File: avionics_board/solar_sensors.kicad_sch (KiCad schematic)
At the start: 4 parts, among them U16 TCA9548APWR, U17 TCA9548APWR

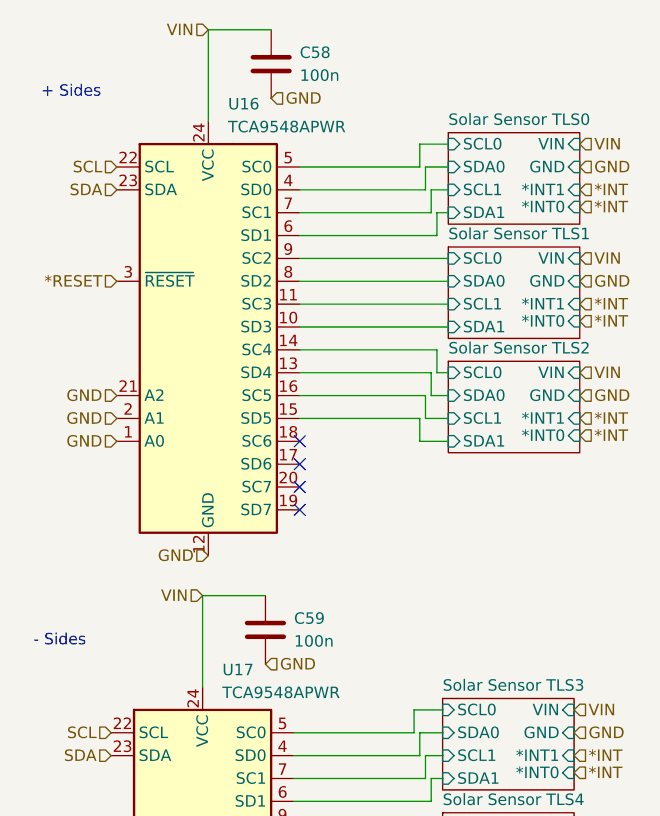
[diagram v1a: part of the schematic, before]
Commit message: reconcile BOMS for AVI. SCI and AUX
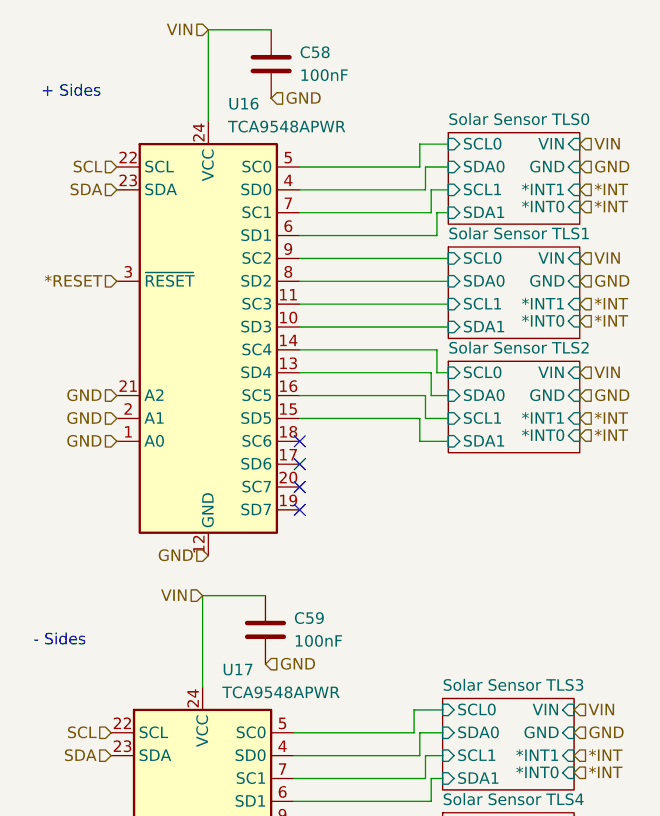
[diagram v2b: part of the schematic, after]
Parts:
- C58, C59: value 100n -> 100nF; Manufacturer (none) -> Murata; Part Number (none) -> GRM155R61E102KA01D; Tolerance (none) -> 10; Voltage (none) -> 25
- U16, U17: Manufacturer (none) -> TI; Part Number (none) -> TCA9548APWR
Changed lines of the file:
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@@
 			)
 		)
-		(property "Value" "100n"
+		(property "Value" "100nF"
 			(at 94.615 123.1899 0)
 			(effects
@@
 			)
 		)
-		(property "Datasheet" "~"
+		(property "Datasheet" "https://search.murata.co.jp/Ceramy/image/img/A01X/G101/ENG/GRM155R61E102KA01-01.pdf"
 			(at 91.44 121.92 0)
 			(effects
@@
 		)
 		(property "Alt" ""
+			(at 91.44 121.92 0)
+			(effects
+				(font
+					(size 1.27 1.27)
+				)
+				(hide yes)
+			)
+		)
+		(property "Manufacturer" "Murata"
+			(at 91.44 121.92 0)
+			(effects
+				(font
+					(size 1.27 1.27)
+				)
+				(hide yes)
+			)
+		)
+		(property "Part Number" "GRM155R61E102KA01D "
+			(at 91.44 121.92 0)
+			(effects
+				(font
+					(size 1.27 1.27)
+				)
+				(hide yes)
+			)
+		)
+		(property "Tolerance" "10"
+			(at 91.44 121.92 0)
+			(effects
+				(font
+					(size 1.27 1.27)
+				)
+				(hide yes)
+			)
+		)
+		(property "Voltage" "25"
 			(at 91.44 121.92 0)
 			(effects
@@
 			)
 		)
-		(property "Value" "100n"
+		(property "Value" "100nF"
 			(at 95.25 60.3249 0)
 			(effects
@@
 			)
 		)
-		(property "Datasheet" "~"
+		(property "Datasheet" "https://search.murata.co.jp/Ceramy/image/img/A01X/G101/ENG/GRM155R61E102KA01-01.pdf"
 			(at 92.075 59.055 0)
 			(effects
@@
 		)
 		(property "Alt" ""
+			(at 92.075 59.055 0)
+			(effects
+				(font
+					(size 1.27 1.27)
+				)
+				(hide yes)
+			)
+		)
+		(property "Manufacturer" "Murata"
+			(at 92.075 59.055 0)
+			(effects
+				(font
+					(size 1.27 1.27)
+				)
+				(hide yes)
+			)
+		)
+		(property "Part Number" "GRM155R61E102KA01D "
+			(at 92.075 59.055 0)
+			(effects
+				(font
+					(size 1.27 1.27)
+				)
+				(hide yes)
+			)
+		)
+		(property "Tolerance" "10"
+			(at 92.075 59.055 0)
+			(effects
+				(font
+					(size 1.27 1.27)
+				)
+				(hide yes)
+			)
+		)
+		(property "Voltage" "25"
 			(at 92.075 59.055 0)
 			(effects
@@
 			)
 		)
+		(property "Manufacturer" "TI"
+			(at 85.09 88.265 0)
+			(effects
+				(font
+					(size 1.27 1.27)
+				)
+				(hide yes)
+			)
+		)
+		(property "Part Number" "TCA9548APWR"
+			(at 85.09 88.265 0)
+			(effects
+				(font
+					(size 1.27 1.27)
+				)
+				(hide yes)
+			)
+		)
 		(pin "24"
 		)
@@
 			(at 84.455 151.13 0)
 			(effects
+				(font
+					(size 1.27 1.27)
+				)
+				(hide yes)
+			)
+		)
+		(property "Manufacturer" "TI"
+			(at 84.455 151.13 0)
+			(effects
+				(font
+					(size 1.27 1.27)
+				)
+				(hide yes)
+			)
+		)
+		(property "Part Number" "TCA9548APWR"
+			(at 84.455 151.13 0)
+			(effects

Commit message: interim checkin for EPS BOM
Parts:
- C58, C59: Part Number GRM155R61E102KA01D -> GRM155R61E104KA87D
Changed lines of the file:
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@@
 			)
 		)
-		(property "Datasheet" "https://search.murata.co.jp/Ceramy/image/img/A01X/G101/ENG/GRM155R61E102KA01-01.pdf"
+		(property "Datasheet" "https://search.murata.co.jp/Ceramy/image/img/A01X/G101/ENG/GRM155R61E104KA87-01.pdf"
 			(at 91.44 121.92 0)
 			(effects
@@
 			)
 		)
-		(property "Part Number" "GRM155R61E102KA01D "
+		(property "Part Number" "GRM155R61E104KA87D"
 			(at 91.44 121.92 0)
 			(effects
@@
 			)
 		)
-		(property "Datasheet" "https://search.murata.co.jp/Ceramy/image/img/A01X/G101/ENG/GRM155R61E102KA01-01.pdf"
+		(property "Datasheet" "https://search.murata.co.jp/Ceramy/image/img/A01X/G101/ENG/GRM155R61E104KA87-01.pdf"
 			(at 92.075 59.055 0)
 			(effects
@@
 			)
 		)
-		(property "Part Number" "GRM155R61E102KA01D "
+		(property "Part Number" "GRM155R61E104KA87D"
 			(at 92.075 59.055 0)
 			(effects

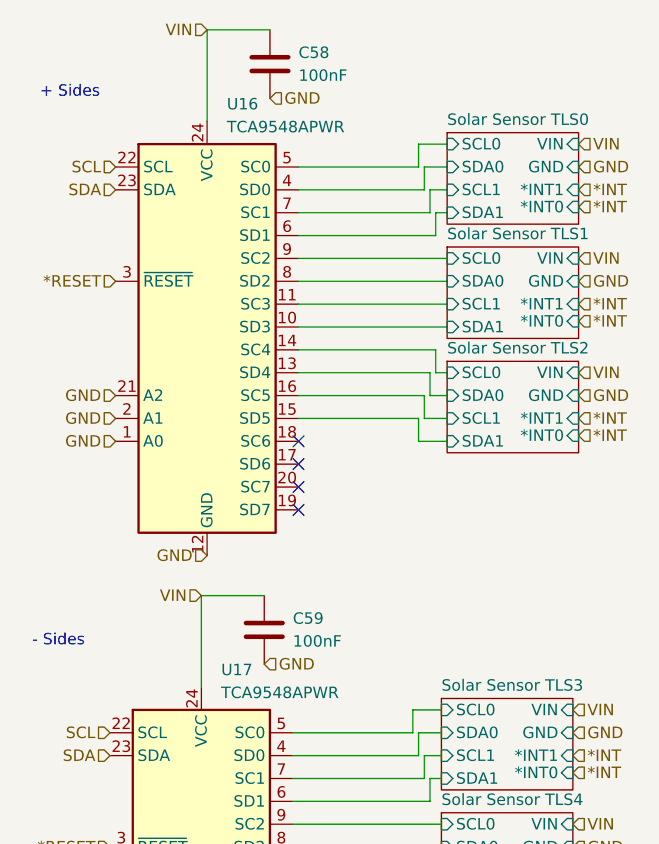
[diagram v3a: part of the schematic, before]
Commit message: reenumerate AVI board
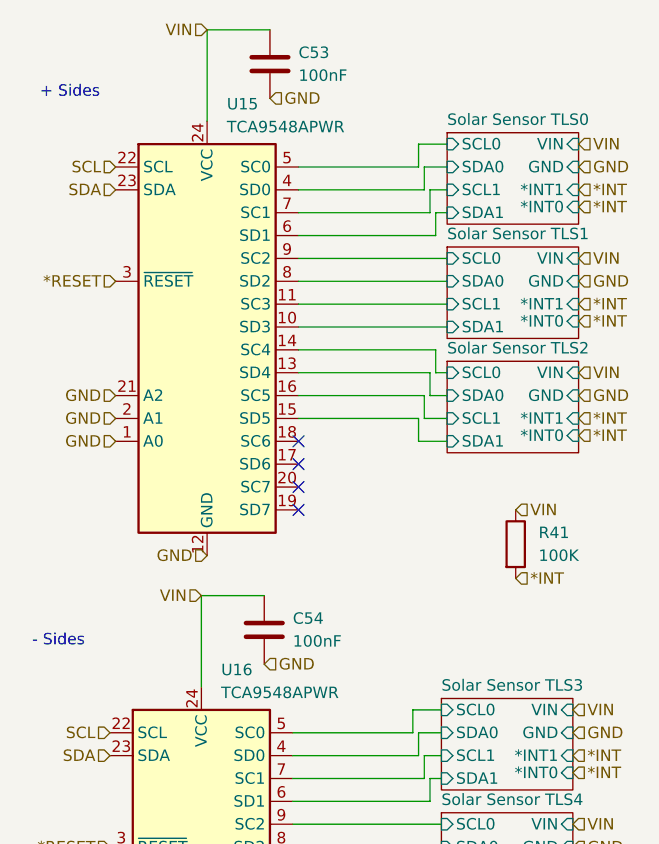
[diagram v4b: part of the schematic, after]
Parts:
- added R41: 100K, Resistor_SMD:R_0402_1005Metric_Pad0.72x0.64mm_HandSolder, symbol Device:R
- renumbered C58 to C53, C59 to C54, U16 to U15, U17 to U16
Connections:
- net *INT: now also R41.2
- net VIN: now also R41.1
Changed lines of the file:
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@@
+		)
+	)
+	(hierarchical_label "*INT"
+		(shape input)
+		(at 119.38 116.205 0)
+		(fields_autoplaced yes)
+		(effects
+			(font
+				(size 1.27 1.27)
+			)
+			(justify left)
 		)
 	)
@@
 		)
 	)
+	(hierarchical_label "VIN"
+		(shape input)
+		(at 119.38 108.585 0)
+		(fields_autoplaced yes)
+		(effects
+			(font
+				(size 1.27 1.27)
+			)
+			(justify left)
+		)
+	)
 	(hierarchical_label "*INT"
 		(shape input)
@@
 			)
 			(justify left)
+		)
+	)
+	(symbol
+		(lib_id "Device:R")
+		(at 119.38 112.395 0)
+		(unit 1)
+		(exclude_from_sim no)
+		(in_bom yes)
+		(on_board yes)
+		(dnp no)
+		(fields_autoplaced yes)
+		(property "Reference" "R41"
+			(at 121.92 111.1249 0)
+			(effects
+				(font
+					(size 1.27 1.27)
+				)
+				(justify left)
+			)
+		)
+		(property "Value" "100K"
+			(at 121.92 113.6649 0)
+			(effects
+				(font
+					(size 1.27 1.27)
+				)
+				(justify left)
+			)
+		)
+		(property "Footprint" "Resistor_SMD:R_0402_1005Metric_Pad0.72x0.64mm_HandSolder"
+			(at 117.602 112.395 90)
+			(effects
+				(font
+					(size 1.27 1.27)
+				)
+				(hide yes)
+			)
+		)
+		(property "Datasheet" "https://www.yageo.com/upload/media/product/products/datasheet/rchip/PYu-RC_Group_51_RoHS_L_12.pdf"
+			(at 119.38 112.395 0)
+			(effects
+				(font
+					(size 1.27 1.27)
+				)
+				(hide yes)
+			)
+		)
+		(property "Description" "Resistor"
+			(at 119.38 112.395 0)
+			(effects
+				(font
+					(size 1.27 1.27)
+				)
+				(hide yes)
+			)
+		)
+		(property "Manufacturer" "YAGEO"
+			(at 119.38 112.395 0)
+			(effects
+				(font
+					(size 1.27 1.27)
+				)
+				(hide yes)
+			)
+		)
+		(property "Part Number" "RC0402FR-07100KL"
+			(at 119.38 112.395 0)
+			(effects
+				(font
+					(size 1.27 1.27)
+				)
+				(hide yes)
+			)
+		)
+		(property "Tolerance" "1"
+			(at 119.38 112.395 0)
+			(effects
+				(font
+					(size 1.27 1.27)
+				)
+				(hide yes)
+			)
+		)
+		(pin "1"
+		)
+		(pin "2"
+		)
+		(instances
+			(project ""
+				(path "/f6cc00ab-17f1-4973-862f-7ac95fe70668/472a2b3c-f2e4-44b5-9587-658c9c0c9365"
+					(reference "R41")
+					(unit 1)
+				)
+			)
 		)
 	)
@@
 		(dnp no)
 		(fields_autoplaced yes)
-		(property "Reference" "C59"
+		(property "Reference" "C54"
 			(at 94.615 120.6499 0)
 			(effects
@@
 			(project "AVIONICS_BOARD"
 				(path "/f6cc00ab-17f1-4973-862f-7ac95fe70668/472a2b3c-f2e4-44b5-9587-658c9c0c9365"
-					(reference "C59")
+					(reference "C54")
 					(unit 1)
 				)
@@
 		(dnp no)
 		(fields_autoplaced yes)
-		(property "Reference" "C58"
+		(property "Reference" "C53"
 			(at 95.25 57.7849 0)
 			(effects
@@
 			(project "AVIONICS_BOARD"
 				(path "/f6cc00ab-17f1-4973-862f-7ac95fe70668/472a2b3c-f2e4-44b5-9587-658c9c0c9365"
-					(reference "C58")
+					(reference "C53")
 					(unit 1)
 				)
@@
 		(dnp no)
 		(fields_autoplaced yes)
-		(property "Reference" "U16"
+		(property "Reference" "U15"
 			(at 87.2841 63.5 0)
 			(effects
@@
 			(project "AVIONICS_BOARD"
 				(path "/f6cc00ab-17f1-4973-862f-7ac95fe70668/472a2b3c-f2e4-44b5-9587-658c9c0c9365"
-					(reference "U16")
+					(reference "U15")
 					(unit 1)
 				)
@@
 		(dnp no)
 		(fields_autoplaced yes)
-		(property "Reference" "U17"
+		(property "Reference" "U16"
 			(at 86.6491 126.365 0)
 			(effects
@@
 			(project "AVIONICS_BOARD"
 				(path "/f6cc00ab-17f1-4973-862f-7ac95fe70668/472a2b3c-f2e4-44b5-9587-658c9c0c9365"
-					(reference "U17")
+					(reference "U16")
 					(unit 1)
 				)

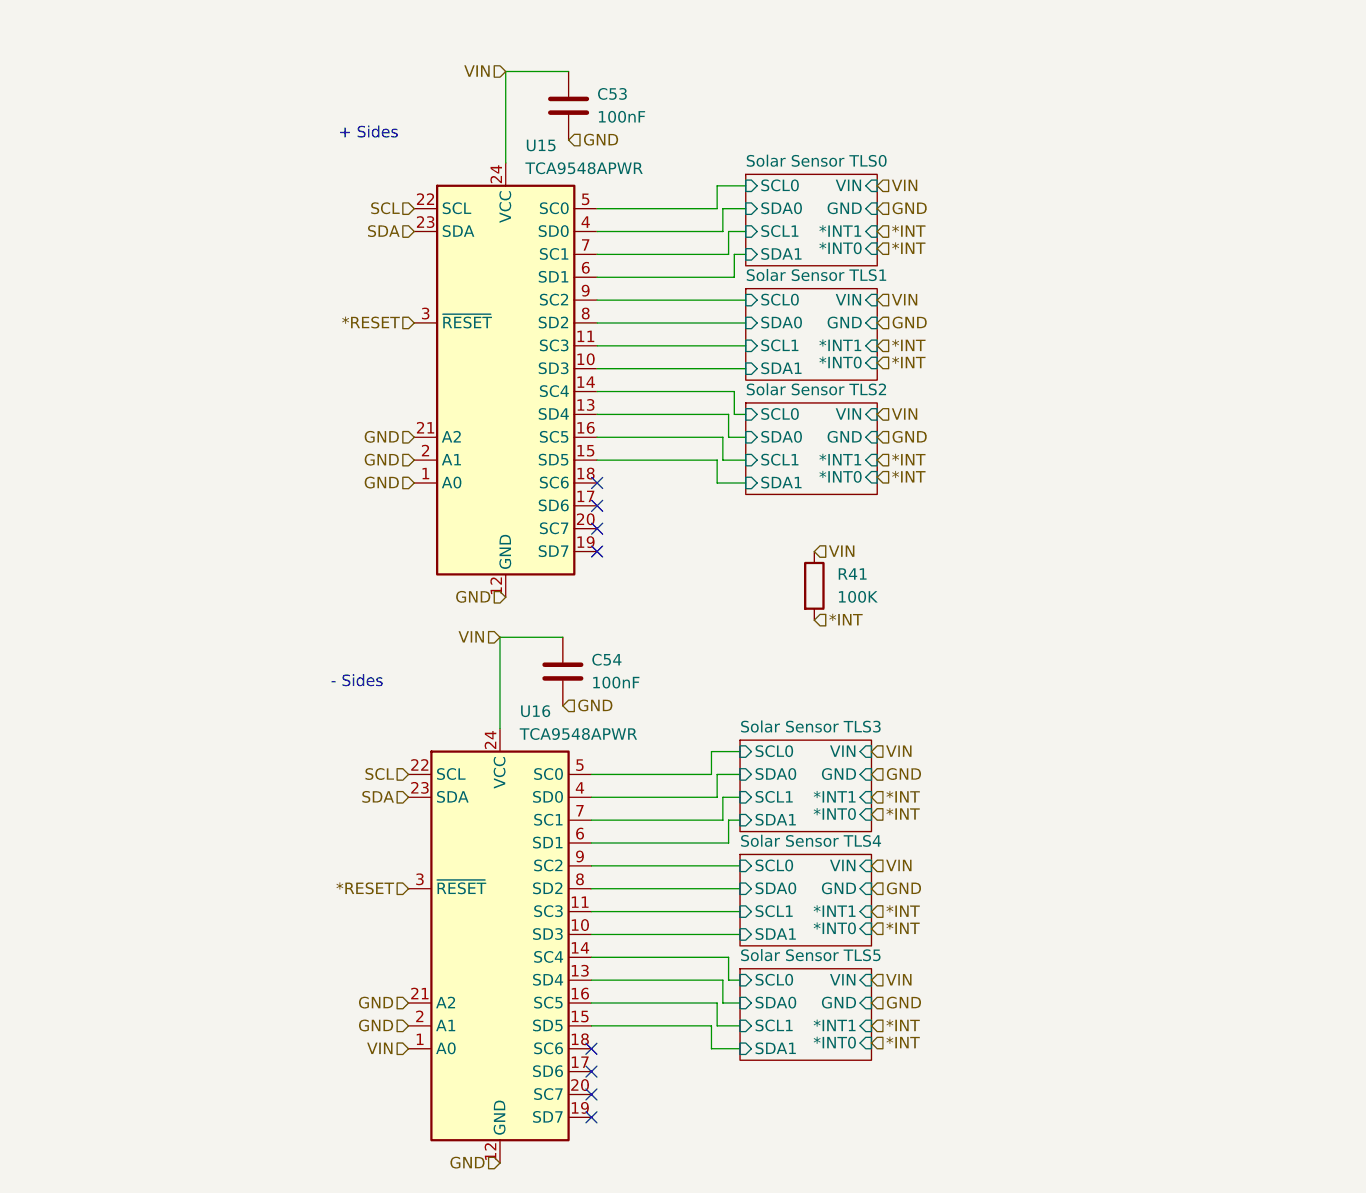
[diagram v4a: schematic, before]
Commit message: use small connectors in corners and on sides for sun sensors and solar cells
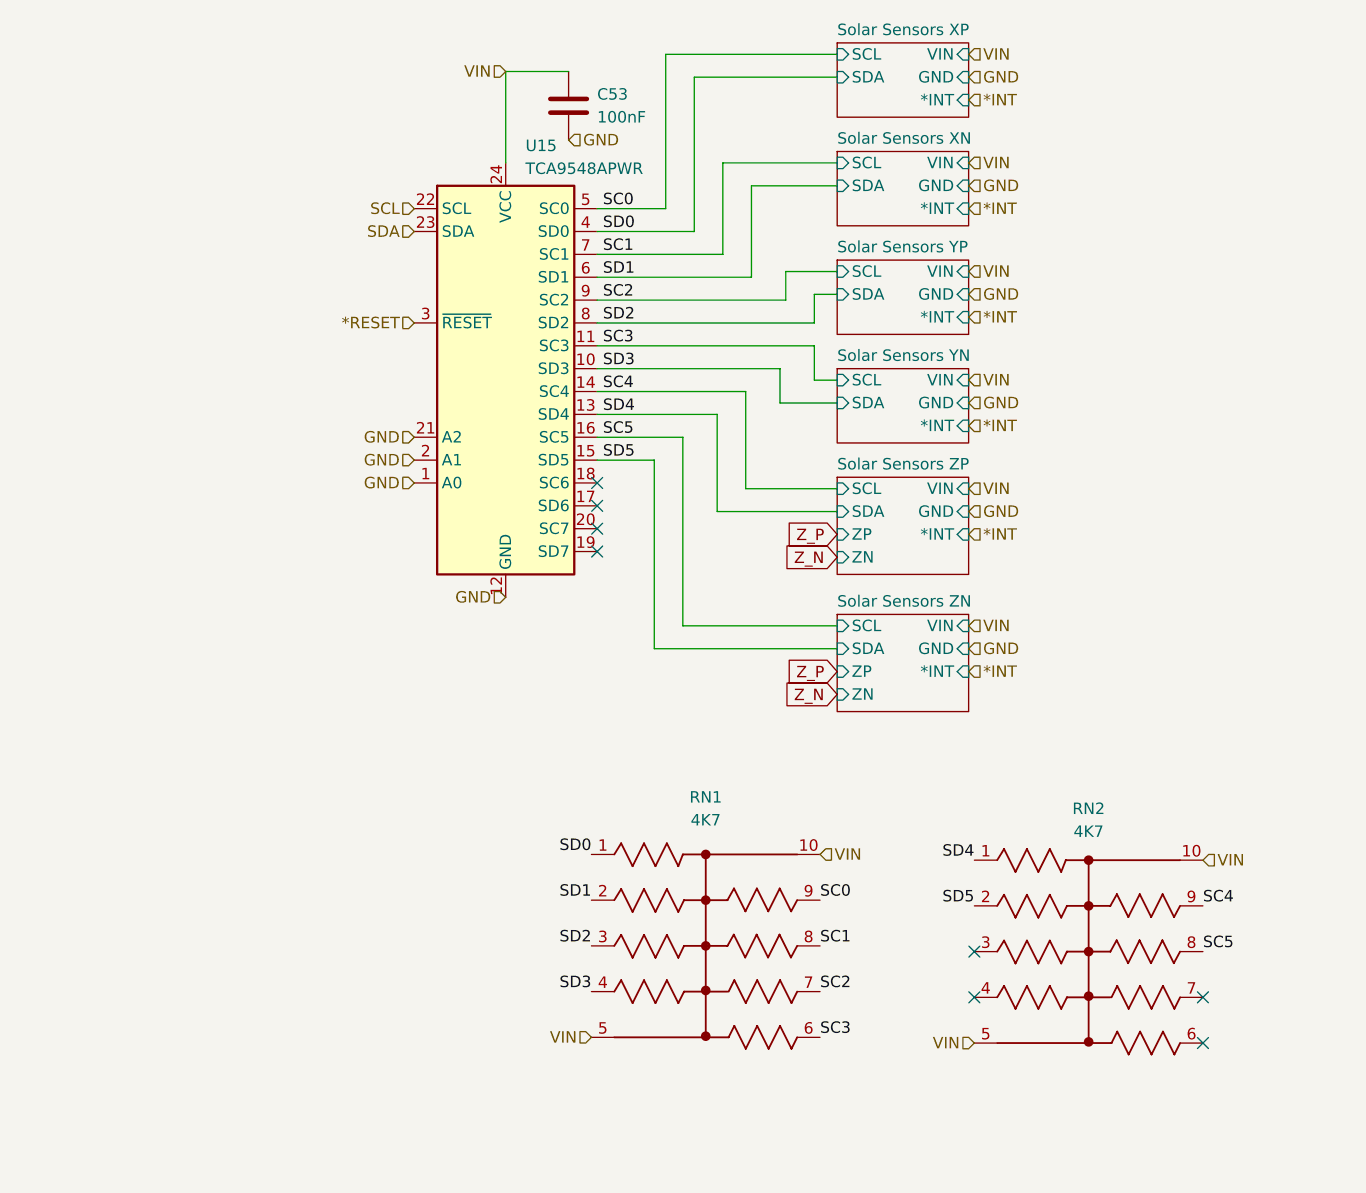
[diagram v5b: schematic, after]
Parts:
- removed C54: 100nF, Capacitor_SMD:C_0402_1005Metric_Pad0.74x0.62mm_HandSolder, symbol Device:C
- removed R41: 100K, Resistor_SMD:R_0402_1005Metric_Pad0.72x0.64mm_HandSolder, symbol Device:R
- removed U16: TCA9548APWR, Package_SO:TSSOP-24_4.4x7.8mm_P0.65mm, symbol Interface_Expansion:TCA9548APWR
- added RN1, RN2: 4K7, Common:C_ARRAY_EXBA_PAN, symbol Common:EXBA10P472J
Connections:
- net VIN: now also RN1.10, RN1.5, RN2.10, RN2.5
- net Solar Sensors XP/SCL0 renamed SC0
- net SC0: now also RN1.9
- net Solar Sensors XP/SCL1 renamed SC1
- net SC1: now also RN1.8
- net Solar Sensors XP/SDA0 renamed SD0
- net SD0: now also RN1.1
- net Solar Sensors XP/SDA1 renamed SD1
- net SD1: now also RN1.2
- net Solar Sensor TLS1/SCL0 renamed SC2
- net SC2: now also RN1.7
- net Solar Sensor TLS1/SCL1 renamed SC3
- net SC3: now also RN1.6
- net Solar Sensor TLS1/SDA0 renamed SD2
- net SD2: now also RN1.3
- net Solar Sensor TLS1/SDA1 renamed SD3
- net SD3: now also RN1.4
- net Solar Sensor TLS2/SCL0 renamed SC4
- net SC4: now also RN2.9
- net Solar Sensor TLS2/SCL1 renamed SC5
- net SC5: now also RN2.8
- net Solar Sensor TLS2/SDA0 renamed SD4
- net SD4: now also RN2.1
- net Solar Sensor TLS2/SDA1 renamed SD5
- net SD5: now also RN2.2
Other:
- sheet Solar Sensor TLS0 renamed Solar Sensors XP
- removed sheet Solar Sensor TLS1
- removed sheet Solar Sensor TLS2
- removed sheet Solar Sensor TLS3
- removed sheet Solar Sensor TLS4
- removed sheet Solar Sensor TLS5
- added sheet Solar Sensors XN (solar_sensor_xy.kicad_sch)
- added sheet Solar Sensors YN (solar_sensor_xy.kicad_sch)
- added sheet Solar Sensors YP (solar_sensor_xy.kicad_sch)
- added sheet Solar Sensors ZN (solar_sensor_z.kicad_sch)
- added sheet Solar Sensors ZP (solar_sensor_z.kicad_sch)
- sheet Solar Sensors XP: file solar_sensor_tls.kicad_sch -> solar_sensor_xy.kicad_sch
- sheet Solar Sensors XP ports: added *INT, SCL, SDA; removed *INT0, *INT1, SCL0, SCL1, SDA0, SDA1
- note removed: "+ Sides"
- note removed: "- Sides"

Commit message: AVI board simplified and cleaned up
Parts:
- added R41, R42: 5K1, Resistor_SMD:R_0402_1005Metric_Pad0.72x0.64mm_HandSolder, symbol Device:R
- R43: renamed from RN1; value 4K7 -> 5K6; AVAILABILITY (none) -> Warning; MF (none) -> Yageo; MOUSER-PURCHASE-URL (none) -> https://snapeda.com/shop?store=Mouser&id=600502; MP (none) -> YC158TJR-0722KL; PACKAGE (none) -> 1206 Yageo; PRICE (none) -> None
- R44: renamed from RN2; value 4K7 -> 5K6; AVAILABILITY (none) -> Warning; MF (none) -> Yageo; MOUSER-PURCHASE-URL (none) -> https://snapeda.com/shop?store=Mouser&id=600502; MP (none) -> YC158TJR-0722KL; PACKAGE (none) -> 1206 Yageo; PRICE (none) -> None
- renumbered C53 to C51, U15 to U13
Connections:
- net SCL: now also R42.2
- net SDA: now also R41.2
- net VIN: now also R41.1, R42.1
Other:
- moved on the sheet: R43, R44

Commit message: EPS and AVI joint cleanup
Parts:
- removed R41, R42: 5K1, Resistor_SMD:R_0402_1005Metric_Pad0.72x0.64mm_HandSolder, symbol Device:R
- renumbered R43 to R39, R44 to R40
